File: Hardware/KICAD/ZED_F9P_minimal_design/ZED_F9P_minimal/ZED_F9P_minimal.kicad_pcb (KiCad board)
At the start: 2 copper layers, 65.2 x 44.5 mm, 28 parts, among them J1 Conn_Coaxial_Small, J2 DF11-18DS-2DSA06, U1 OPA2365AID, U2 LM1086IT-ADJ/NOPB, U3 ZED-F9P

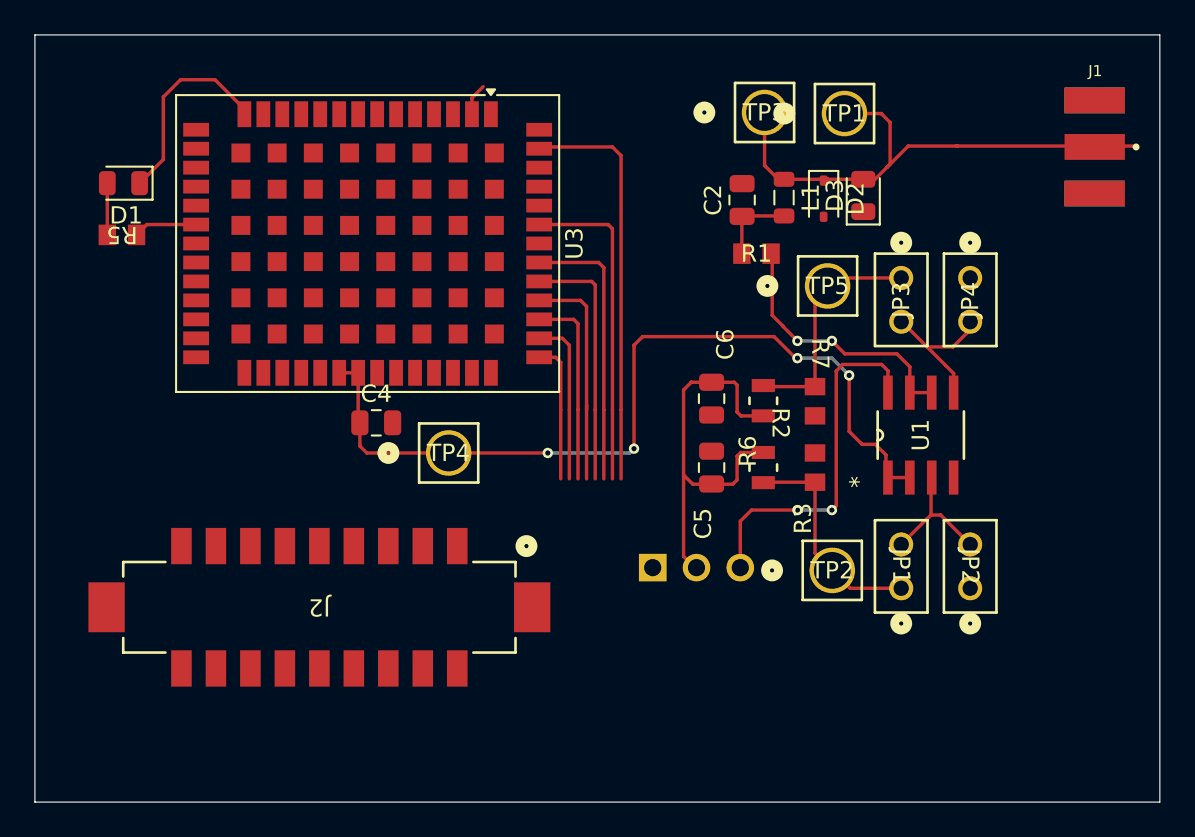
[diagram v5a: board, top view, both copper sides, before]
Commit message: rooting PCB
added ground plane, rooted and shaped critical input signal for 50ohm impedance
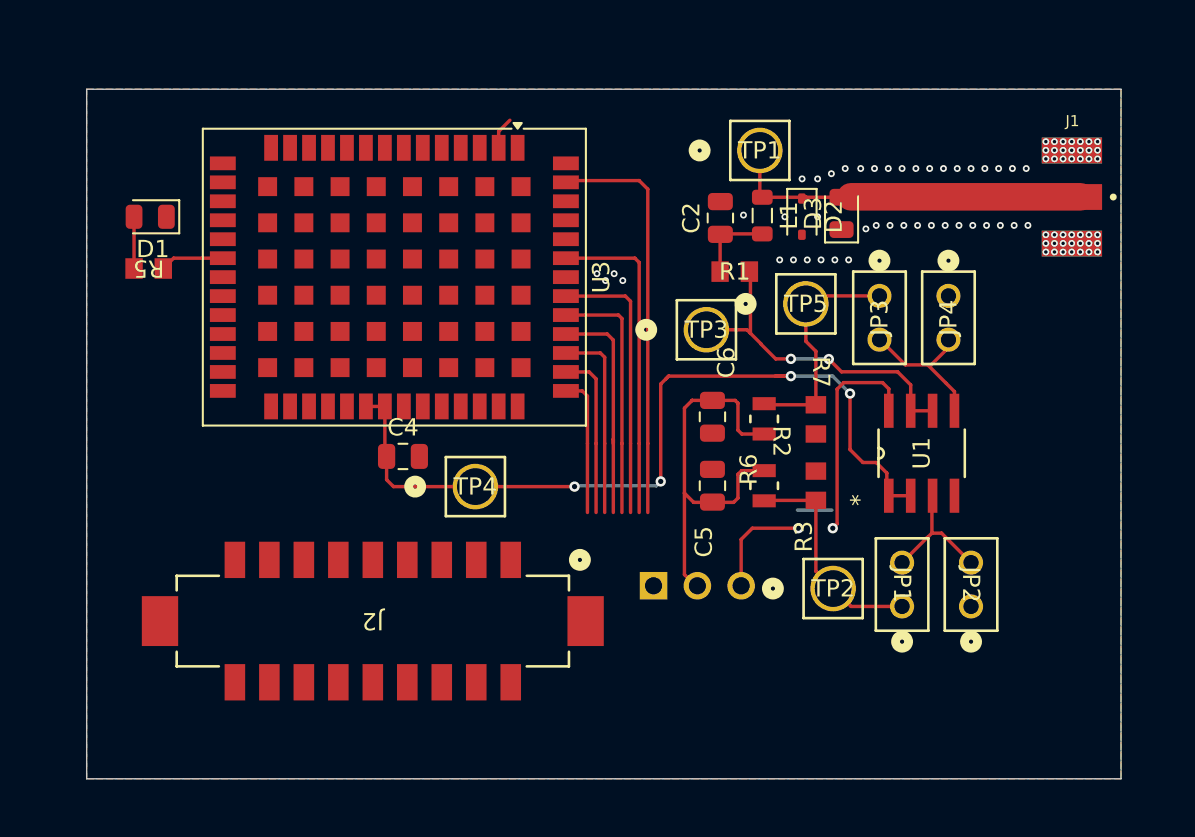
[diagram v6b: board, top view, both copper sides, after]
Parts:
- moved TP3 13.0 mm to (56.0, 34.0)
- moved TP1 5.36 mm to (59.0, 23.6)
- moved J2 3.20 mm to (36.6, 50.9)
- moved J1 3.19 mm to (77.2, 26.3)
- moved U3 2.49 mm to (37.9, 30.9)
- moved D1 2.49 mm to (23.7, 27.4)
- moved C4 2.49 mm to (38.4, 41.3)
- moved R5 2.49 mm to (23.6, 30.4)
- moved TP4 2.49 mm to (42.5, 43.0)
- moved C2 1.64 mm to (56.8, 27.5)
- moved D2 1.64 mm to (61.5, 27.4)
- moved D3 1.64 mm to (63.8, 27.2)
- moved JP3 1.64 mm to (66.0, 32.0)
- moved JP4 1.64 mm to (70.0, 32.0)
- moved L1 1.64 mm to (59.2, 27.3)
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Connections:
- J1 pad G1: (no net) -> GND
- J1 pad G2: (no net) -> GND
- J1 pad G3: (no net) -> GND
- J1 pad G4: (no net) -> GND
- J2 pad 1: /TIMER -> /12V
- J2 pad 10: unconnected-(J2-Pad10) -> GND
- J2 pad 11: unconnected-(J2-Pad11) -> /UART_RX
- J2 pad 12: unconnected-(J2-Pad12) -> /UART_TX
- J2 pad 13: unconnected-(J2-Pad13) -> /I/O 
- J2 pad 14: unconnected-(J2-Pad14) -> /I/O_CLK_SELECT
- J2 pad 15: unconnected-(J2-Pad15) -> /O_TX_STATE
- J2 pad 16: /5V-jumper -> /I_D_Sel
- J2 pad 17: /3V3-jumper -> /I_RESET
- J2 pad 18: /12V -> /TIMER
- J2 pad 2: /I_RESET -> /3V3-jumper
- J2 pad 3: /I_D_Sel -> /5V-jumper
- J2 pad 4: /O_TX_STATE -> unconnected-(J2-Pad4)
- J2 pad 5: /I/O_CLK_SELECT -> unconnected-(J2-Pad5)
- J2 pad 6: /I/O  -> unconnected-(J2-Pad6)
- J2 pad 7: /UART_TX -> unconnected-(J2-Pad7)
- J2 pad 8: /UART_RX -> unconnected-(J2-Pad8)
- J2 pad 9: GND -> unconnected-(J2-Pad9)
- TP3 pad 1: /RF_IN -> /5v_antenne
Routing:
- net GND: track 12.0 -> 0.65 mm, vias 0 -> 85
- net /RF_IN: track 33.3 -> 23.4 mm
- net /5v_antenne: track 16.0 -> 19.9 mm
- net /3v3_puce: track 49.8 -> 48.5 mm
- net /5V-IN: track 13.6 -> 14.6 mm
- added copper zone on B.Cu, net GND
- added copper zone on F.Cu, net GND
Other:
- board size 65.2 x 44.5 mm -> 60 x 40 mm

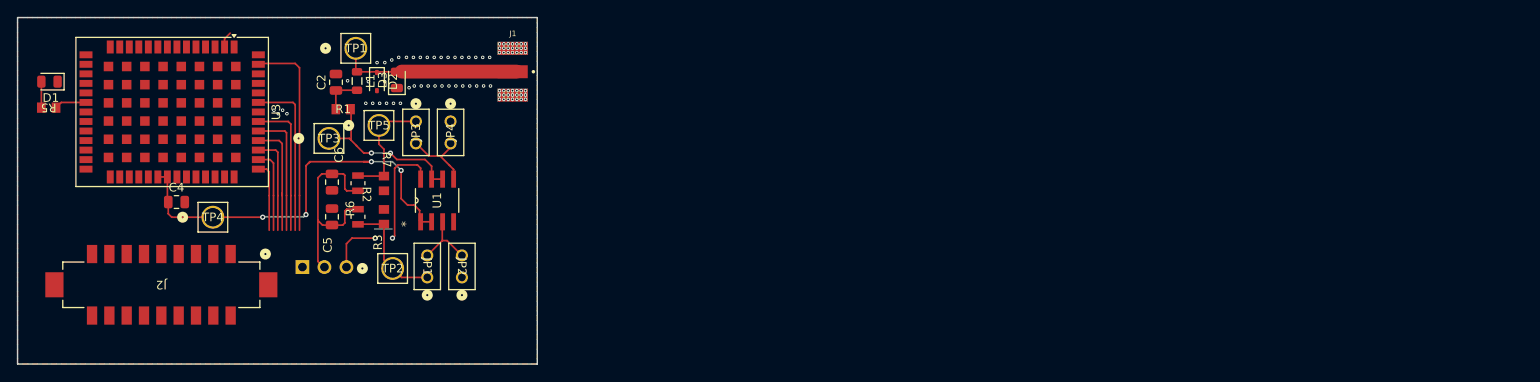
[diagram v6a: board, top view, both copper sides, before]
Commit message: corrections
added SMA connector and  actualised pin connector footprint
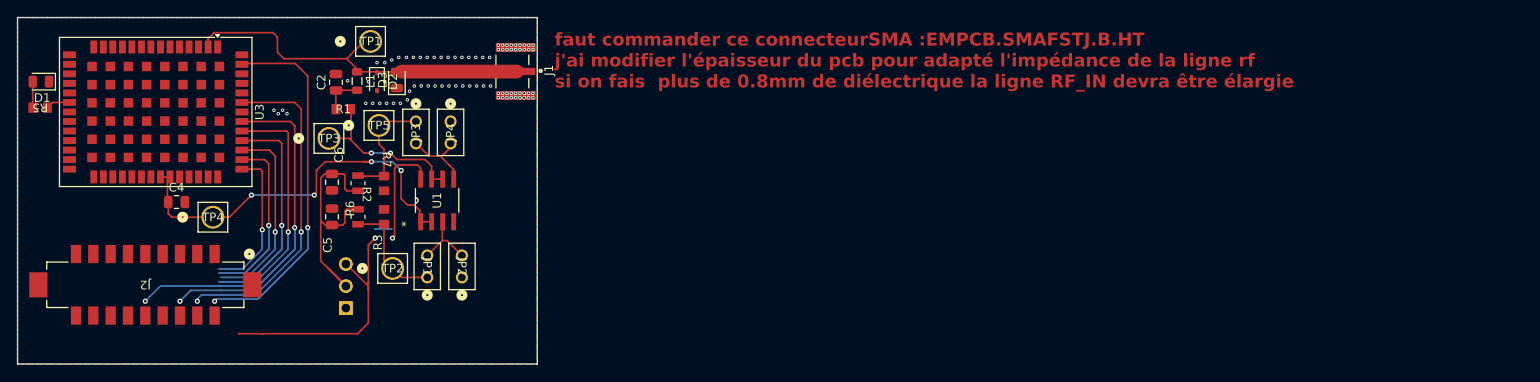
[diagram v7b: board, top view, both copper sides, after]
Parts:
- J1: value Conn_Coaxial_Small -> EMPCB.SMAFSTJ.B.HT; footprint SMA:RFSOLUTIONS_CON-SMA-EDGE-S -> Connector:TAOGLAS_EMPCB.SMAFSTJ.B.HT
- moved U2 3.31 mm to (57.9, 51.0), turned to 90 degrees
- moved U3 1.90 mm to (36.0, 30.9)
- moved TP1 1.88 mm to (60.8, 22.8)
- moved J2 1.85 mm to (34.8, 50.9)
- moved D1 1.00 mm to (22.7, 27.4)
- moved R5 1.00 mm to (22.6, 30.4)
- moved J1 0.35 mm to (77.5, 26.2), turned to -90 degrees
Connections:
- J2 pad 19: (no net) -> GND
- J2 pad 20: (no net) -> GND
- J2 pad 4: unconnected-(J2-Pad4) -> GND
- J2 pad 5: unconnected-(J2-Pad5) -> GND
- J2 pad 6: unconnected-(J2-Pad6) -> GND
- J2 pad 7: unconnected-(J2-Pad7) -> GND
- J2 pad 8: unconnected-(J2-Pad8) -> GND
- J2 pad 9: unconnected-(J2-Pad9) -> GND
- R5 pad 1: Net-(U3-RTK_STAT) -> GND
- U3 pad 19: unconnected-(U3-GEOFENCE_STAT-Pad19) -> GND
- U3 pad 20: Net-(U3-RTK_STAT) -> GND
- U3 pad 26: unconnected-(U3-RXD2-Pad26) -> GND
- U3 pad 27: unconnected-(U3-TXD2-Pad27) -> GND
- U3 pad 4: unconnected-(U3-ANT_DETECT-Pad4) -> GND
- U3 pad 5: unconnected-(U3-ANT_OFF-Pad5) -> GND
- U3 pad 50: unconnected-(U3-~{SAFEBOOT}-Pad50) -> GND
- U3 pad 51: unconnected-(U3-EXTINT-Pad51) -> GND
- U3 pad 6: unconnected-(U3-~{ANT_SHORT}-Pad6) -> GND
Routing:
- net /12V: track 21.0 -> 44.7 mm
- net /O_TX_STATE: track 14.6 -> 37.9 mm, vias 0 -> 2
- net /RF_IN: track 23.4 -> 44.0 mm
- net /I_D_Sel: track 16.1 -> 36.3 mm, vias 0 -> 2
- net /I_RESET: track 18.9 -> 38.0 mm, vias 0 -> 2
- net /TIMER: track 23.7 -> 41.5 mm, vias 0 -> 2
- net /I/O_CLK_SELECT: track 13.1 -> 25.8 mm, vias 0 -> 1
- net /I/O : track 11.4 -> 23.0 mm, vias 0 -> 1
- net /UART_RX: track 9.67 -> 20.6 mm, vias 0 -> 1
- net /UART_TX: track 8.12 -> 17.9 mm, vias 0 -> 1
- net Net-(U2-OUTPUT): track 24.2 -> 30.3 mm
- net Net-(U3-RTK_STAT): track 3.70 -> 0.00 mm
- net GND: track 0.65 -> 3.45 mm, vias 85 -> 82
- net /3v3_puce: track 48.5 -> 46.5 mm
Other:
- board text added: "faut commander ce connecteurSMA :EMPCB.SMAFSTJ.B.HT j'ai modifier l'épaisseur du pcb pour adapté l'impédance de la ligne rf si on fais plus de 0.8mm de diélectrique la ligne RF_IN devra être élargie"

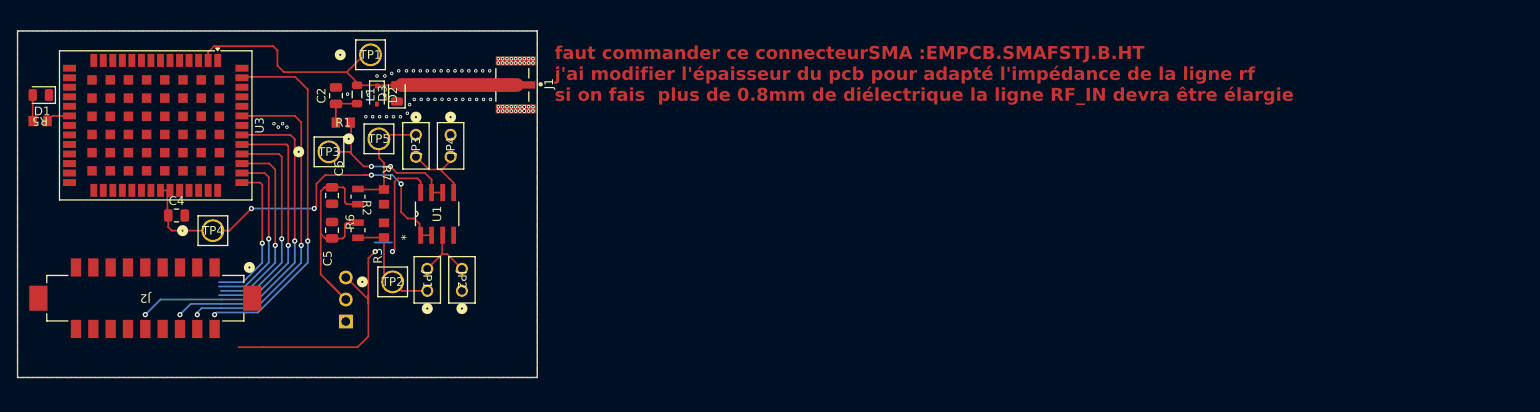
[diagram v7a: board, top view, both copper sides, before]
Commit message: PCB rooting
finalised PCB rooting
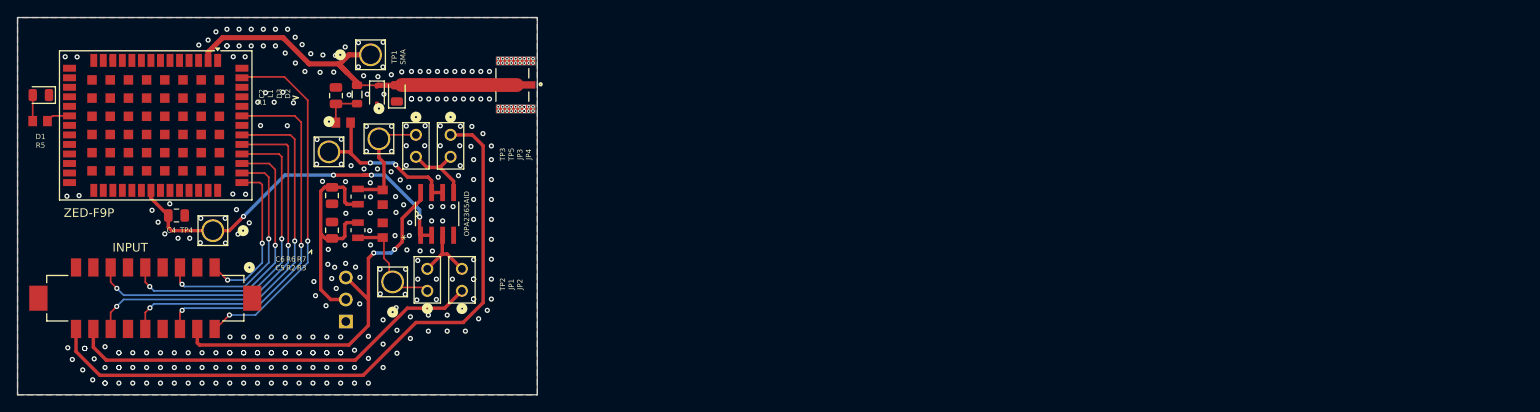
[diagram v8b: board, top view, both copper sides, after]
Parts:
- moved R7 0.16 mm to (62.1, 39.2)
- moved R3 0.15 mm to (62.1, 43.0)
- turned TP2 to 90 degrees
- turned TP3 to -90 degrees
- turned TP4 to 180 degrees
- turned TP5 to -90 degrees
- renumbered J2 to INPUT, U1 to OPA2365AID, J1 to SMA, U3 to ZED-F9P
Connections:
- net Net-(U2-OUTPUT) renamed /pt div
- INPUT pad 1: /12V -> /UART_TX
- INPUT pad 10: GND -> /I_D_Sel
- INPUT pad 11: /UART_RX -> GND
- INPUT pad 12: /UART_TX -> GND
- INPUT pad 13: /I/O  -> /I/O_CLK_SELECT
- INPUT pad 14: /I/O_CLK_SELECT -> /O_TX_STATE
- INPUT pad 15: /O_TX_STATE -> GND
- INPUT pad 16: /I_D_Sel -> /3V3-jumper
- INPUT pad 17: /I_RESET -> GND
- INPUT pad 18: /TIMER -> /5V-jumper
- INPUT pad 19: GND -> (no net)
- INPUT pad 2: /3V3-jumper -> /TIMER
- INPUT pad 20: GND -> (no net)
- INPUT pad 3: /5V-jumper -> GND
- INPUT pad 4: GND -> /12V
- INPUT pad 5: GND -> /UART_RX
- INPUT pad 6: GND -> /I_RESET
- INPUT pad 9: GND -> /I/O 
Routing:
- net /5V-jumper: track 0.00 -> 76.6 mm
- net /3V3-jumper: track 0.00 -> 48.6 mm
- net /I/O_CLK_SELECT: track 25.8 -> 40.6 mm, vias 1 -> 2
- net /I/O : track 23.0 -> 33.9 mm, vias 1 -> 2
- net /UART_RX: track 20.6 -> 27.0 mm, vias 1 -> 2
- net /I_D_Sel: track 36.3 -> 42.1 mm
- net /O_TX_STATE: track 37.9 -> 43.7 mm
- net /I_RESET: track 38.0 -> 41.6 mm
- net /3v3_puce: track 46.5 -> 43.7 mm
- net /pt div: track 30.3 -> 27.8 mm
- net /RF_IN: track 44.0 -> 45.6 mm
- net /12V: track 44.7 -> 45.7 mm
- net /UART_TX: track 17.9 -> 18.9 mm, vias 1 -> 2
- net GND: vias 82 -> 322
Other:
- board size 60 x 40 mm -> 60 x 43.5 mm
- board text removed: "faut commander ce connecteurSMA :EMPCB.SMAFSTJ.B.HT j'ai modifier l'épaisseur du pcb pour adapté l'impédance de la ligne rf si on fais plus de 0.8mm de diélectrique la ligne RF_IN devra être élargie"
